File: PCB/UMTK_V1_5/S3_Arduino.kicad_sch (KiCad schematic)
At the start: 30 parts

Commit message: Routing and JLC Assignment Done
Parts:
- removed R2, R3, R6, R7: 10k, Resistor_SMD:R_0402_1005Metric, symbol Device:R_US
- R1, R5: value 10k -> 100k
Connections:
- net VM_Sense: now also R5.2
- net Vin_Sense: now also R1.2
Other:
- moved on the sheet: R1, R5

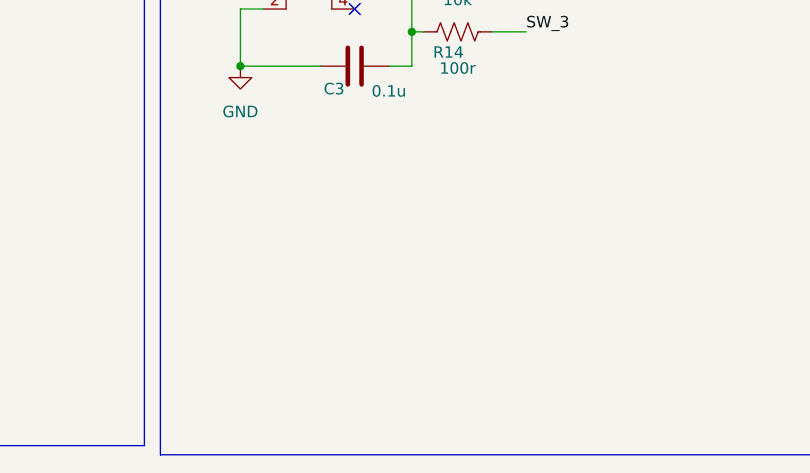
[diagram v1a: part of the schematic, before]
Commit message: Bug fixes and add dummy headers for DFM
Fix:
- Power jack footprint incorrect for high current jack
- Motor and Estop terminal hole size too small
- Added designator and position for arduino headers for DFM
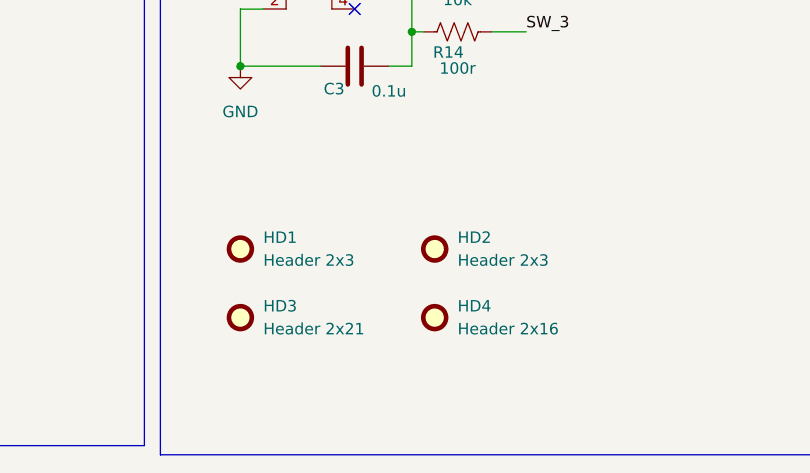
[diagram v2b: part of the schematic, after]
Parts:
- added HD1, HD2: Header 2x3, AMX_Logo:Dummy_Header_2x3, symbol Mechanical:Fiducial
- added HD3: Header 2x21, AMX_Logo:Dummy_Header_2x21, symbol Mechanical:Fiducial
- added HD4: Header 2x16, AMX_Logo:Dummy_Header_2x16, symbol Mechanical:Fiducial

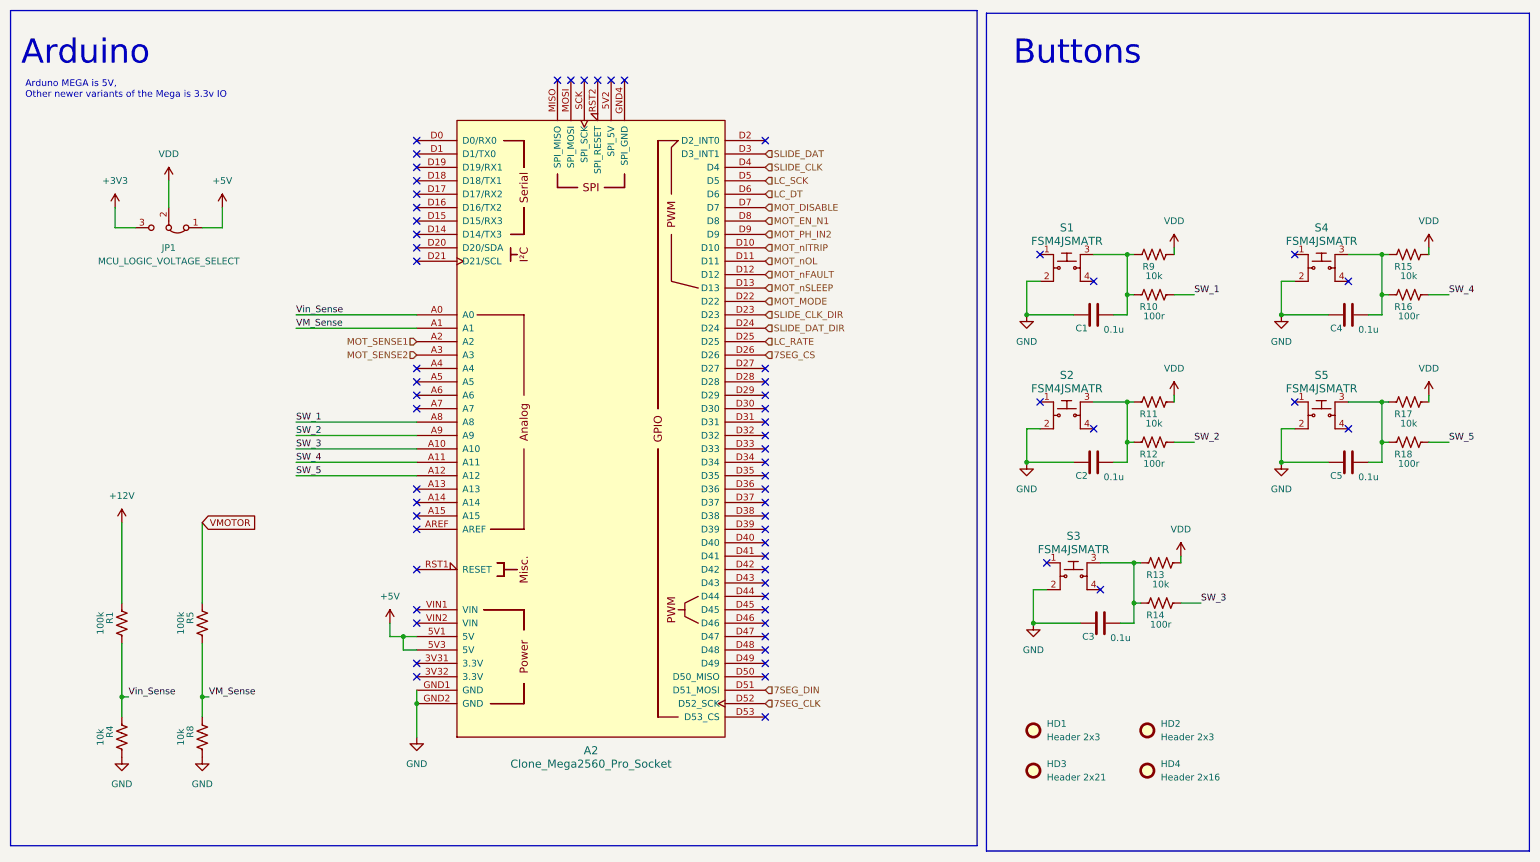
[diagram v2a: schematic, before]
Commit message: Added pin assignment doc for firmware
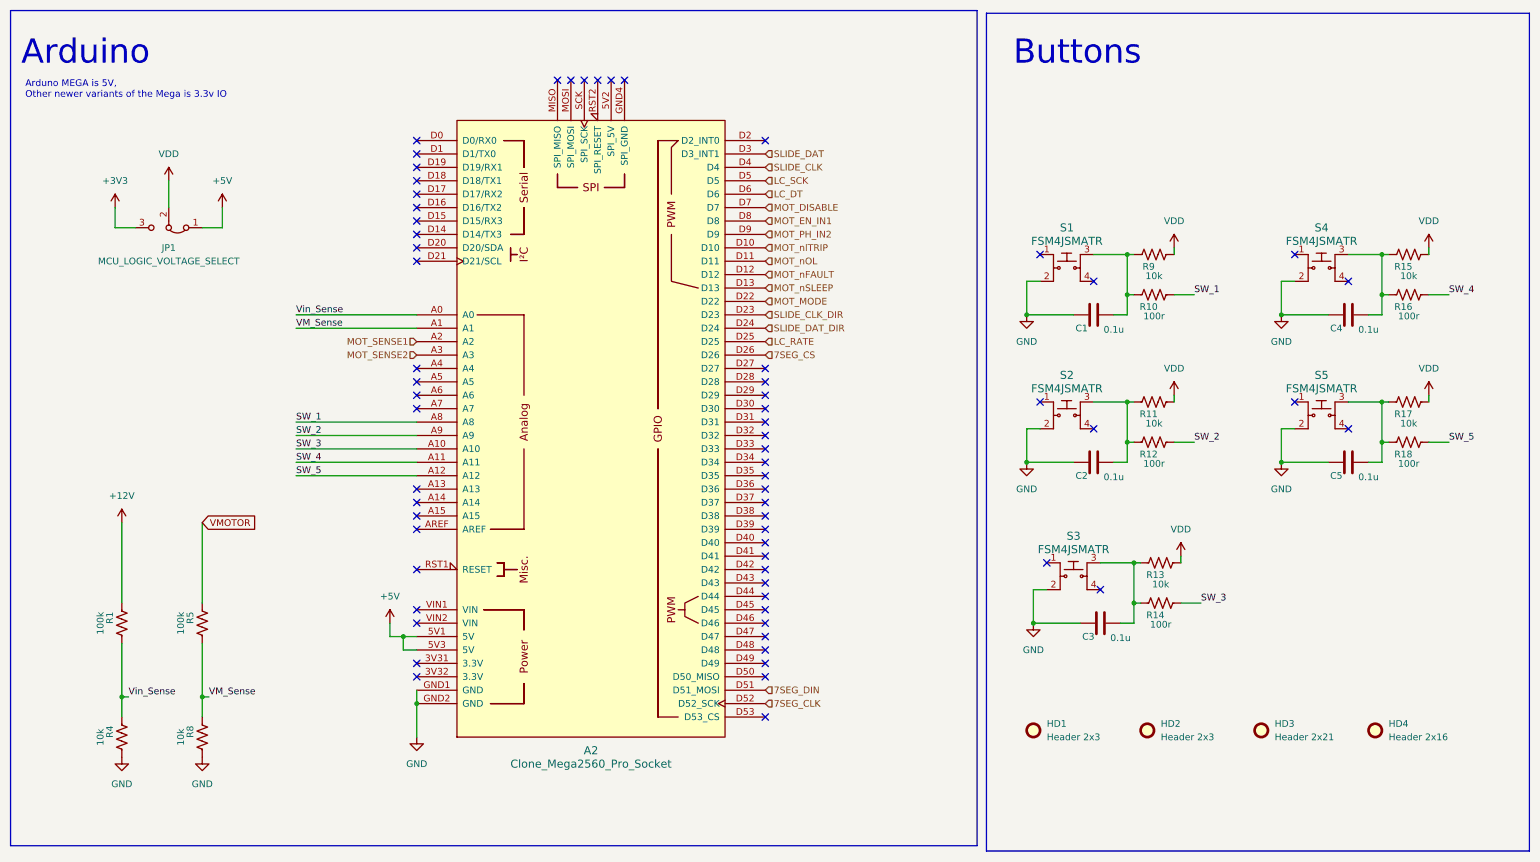
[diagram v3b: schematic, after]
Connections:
- net MOT_EN_N1 renamed MOT_EN_IN1
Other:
- moved on the sheet: HD3, HD4
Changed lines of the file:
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@@
 		)
 	)
-	(hierarchical_label "MOT_EN_N1"
+	(hierarchical_label "MOT_EN_IN1"
 		(shape input)
 		(at 147.32 59.69 0)
@@
 	(symbol
 		(lib_id "Mechanical:Fiducial")
-		(at 219.71 163.83 0)
+		(at 262.89 156.21 0)
 		(unit 1)
 		(exclude_from_sim yes)
@@
 		(fields_autoplaced yes)
 		(property "Reference" "HD4"
-			(at 222.25 162.5599 0)
+			(at 265.43 154.9399 0)
 			(effects
 				(font
@@
 		)
 		(property "Value" "Header 2x16"
-			(at 222.25 165.0999 0)
+			(at 265.43 157.4799 0)
 			(effects
 				(font
@@
 		)
 		(property "Footprint" "AMX_Logo:Dummy_Header_2x16"
-			(at 219.71 163.83 0)
+			(at 262.89 156.21 0)
 			(effects
 				(font
@@
 		)
 		(property "Datasheet" "~"
-			(at 219.71 163.83 0)
+			(at 262.89 156.21 0)
 			(effects
 				(font
@@
 		)
 		(property "Description" "Fiducial Marker"
-			(at 219.71 163.83 0)
+			(at 262.89 156.21 0)
 			(effects
 				(font
@@
 	(symbol
 		(lib_id "Mechanical:Fiducial")
-		(at 198.12 163.83 0)
+		(at 241.3 156.21 0)
 		(unit 1)
 		(exclude_from_sim yes)
@@
 		(fields_autoplaced yes)
 		(property "Reference" "HD3"
-			(at 200.66 162.5599 0)
+			(at 243.84 154.9399 0)
 			(effects
 				(font
@@
 		)
 		(property "Value" "Header 2x21"
-			(at 200.66 165.0999 0)
+			(at 243.84 157.4799 0)
 			(effects
 				(font
@@
 		)
 		(property "Footprint" "AMX_Logo:Dummy_Header_2x21"
-			(at 198.12 163.83 0)
+			(at 241.3 156.21 0)
 			(effects
 				(font
@@
 		)
 		(property "Datasheet" "~"
-			(at 198.12 163.83 0)
+			(at 241.3 156.21 0)
 			(effects
 				(font
@@
 		)
 		(property "Description" "Fiducial Marker"
-			(at 198.12 163.83 0)
-			(effects
-				(font
+			(at 241.3 156.21 0)
+			(effects
+				(font

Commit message: Make simple components bigger
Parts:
- C1, C2, C3, C4, C5: footprint Capacitor_SMD:C_0402_1005Metric -> Capacitor_SMD:C_0603_1608Metric
- R1, R10, R11, R12, R13, R14, R15, R16, R17, R18, R4, R5, R8, R9: footprint Resistor_SMD:R_0402_1005Metric -> Resistor_SMD:R_0603_1608Metric
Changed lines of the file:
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@@
 			)
 		)
-		(property "Footprint" "Resistor_SMD:R_0402_1005Metric"
+		(property "Footprint" "Resistor_SMD:R_0603_1608Metric"
 			(at 222.504 131.064 90)
 			(effects
@@
 			)
 		)
-		(property "Footprint" "Capacitor_SMD:C_0402_1005Metric"
+		(property "Footprint" "Capacitor_SMD:C_0603_1608Metric"
 			(at 261.62 76.5048 0)
 			(effects
@@
 			)
 		)
-		(property "Footprint" "Resistor_SMD:R_0402_1005Metric"
+		(property "Footprint" "Resistor_SMD:R_0603_1608Metric"
 			(at 269.494 65.024 90)
 			(effects
@@
 			)
 		)
-		(property "Footprint" "Resistor_SMD:R_0402_1005Metric"
+		(property "Footprint" "Resistor_SMD:R_0603_1608Metric"
 			(at 26.416 157.734 90)
 			(effects
@@
 			)
 		)
-		(property "Footprint" "Resistor_SMD:R_0402_1005Metric"
+		(property "Footprint" "Resistor_SMD:R_0603_1608Metric"
 			(at 269.494 92.964 90)
 			(effects
@@
 			)
 		)
-		(property "Footprint" "Capacitor_SMD:C_0402_1005Metric"
+		(property "Footprint" "Capacitor_SMD:C_0603_1608Metric"
 			(at 261.62 104.4448 0)
 			(effects
@@
 			)
 		)
-		(property "Footprint" "Capacitor_SMD:C_0402_1005Metric"
+		(property "Footprint" "Capacitor_SMD:C_0603_1608Metric"
 			(at 213.36 76.5048 0)
 			(effects
@@
 			)
 		)
-		(property "Footprint" "Resistor_SMD:R_0402_1005Metric"
+		(property "Footprint" "Resistor_SMD:R_0603_1608Metric"
 			(at 221.234 92.964 90)
 			(effects
@@
 			)
 		)
-		(property "Footprint" "Resistor_SMD:R_0402_1005Metric"
+		(property "Footprint" "Resistor_SMD:R_0603_1608Metric"
 			(at 41.656 157.734 90)
 			(effects
@@
 			)
 		)
-		(property "Footprint" "Resistor_SMD:R_0402_1005Metric"
+		(property "Footprint" "Resistor_SMD:R_0603_1608Metric"
 			(at 269.494 100.584 90)
 			(effects
@@
 			)
 		)
-		(property "Footprint" "Resistor_SMD:R_0402_1005Metric"
+		(property "Footprint" "Resistor_SMD:R_0603_1608Metric"
 			(at 41.656 136.144 90)
 			(effects
@@
 			)
 		)
-		(property "Footprint" "Resistor_SMD:R_0402_1005Metric"
+		(property "Footprint" "Resistor_SMD:R_0603_1608Metric"
 			(at 221.234 100.584 90)
 			(effects
@@
 			)
 		)
-		(property "Footprint" "Capacitor_SMD:C_0402_1005Metric"
+		(property "Footprint" "Capacitor_SMD:C_0603_1608Metric"
 			(at 213.36 104.4448 0)
 			(effects
@@
 			)
 		)
-		(property "Footprint" "Resistor_SMD:R_0402_1005Metric"
+		(property "Footprint" "Resistor_SMD:R_0603_1608Metric"
 			(at 269.494 72.644 90)
 			(effects
@@
 			)
 		)
-		(property "Footprint" "Capacitor_SMD:C_0402_1005Metric"
+		(property "Footprint" "Capacitor_SMD:C_0603_1608Metric"
 			(at 214.63 134.9248 0)
 			(effects
@@
 			)
 		)
-		(property "Footprint" "Resistor_SMD:R_0402_1005Metric"
+		(property "Footprint" "Resistor_SMD:R_0603_1608Metric"
 			(at 222.504 123.444 90)
 			(effects
@@
 			)
 		)
-		(property "Footprint" "Resistor_SMD:R_0402_1005Metric"
+		(property "Footprint" "Resistor_SMD:R_0603_1608Metric"
 			(at 221.234 65.024 90)
 			(effects
@@
 			)
 		)
-		(property "Footprint" "Resistor_SMD:R_0402_1005Metric"
+		(property "Footprint" "Resistor_SMD:R_0603_1608Metric"
 			(at 221.234 72.644 90)
 			(effects
@@
 			)
 		)
-		(property "Footprint" "Resistor_SMD:R_0402_1005Metric"
+		(property "Footprint" "Resistor_SMD:R_0603_1608Metric"
 			(at 26.416 136.144 90)
 			(effects

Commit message: Move interrupr pin to 3, Move motor sleep to 14 so 13 can LED
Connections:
- net MOT_nSLEEP: now also A2.D14 (D14/TX3); no longer A2.D13
- net SLIDE_CLK: now also A2.D3 (D3_INT1); no longer A2.D4
- net SLIDE_DAT: now also A2.D4; no longer A2.D3 (D3_INT1)
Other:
- note added: "SLIDE REQUIRE INTERRUPT ON MEGA ONLY THESE PINS CAN INTERRUPT: 2, 3, 18, 19"
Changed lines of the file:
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@@
+	)
+	(no_connect
+		(at 147.32 87.63)
 	)
 	(no_connect
@@
 	)
 	(no_connect
-		(at 147.32 87.63)
-	)
-	(no_connect
 		(at 247.65 66.04)
 	)
@@
 	)
 	(no_connect
+		(at 147.32 72.39)
+	)
+	(no_connect
 		(at 147.32 128.27)
 	)
@@
 	(no_connect
 		(at 113.03 33.02)
-	)
-	(no_connect
-		(at 81.28 62.23)
 	)
 	(wire
@@
 		)
 	)
+	(text "SLIDE REQUIRE INTERRUPT\nON MEGA ONLY THESE PINS\nCAN INTERRUPT:\n2, 3, 18, 19"
+		(exclude_from_sim no)
+		(at 149.606 32.258 0)
+		(effects
+			(font
+				(size 1.27 1.27)
+			)
+			(justify left)
+		)
+	)
 	(text "Buttons"
 		(exclude_from_sim no)
@@
 	(label "SW_2"
 		(at 228.6 101.6 0)
+		(fields_autoplaced yes)
+		(effects
+			(font
+				(size 1.27 1.27)
+			)
+			(justify left bottom)
+		)
+	)
+	(label "13 IS INDICATOR LED"
+		(at 148.59 73.66 0)
 		(fields_autoplaced yes)
 		(effects
@@
 		)
 	)
+	(hierarchical_label "SLIDE_CLK"
+		(shape input)
+		(at 147.32 46.99 0)
+		(fields_autoplaced yes)
+		(effects
+			(font
+				(size 1.27 1.27)
+			)
+			(justify left)
+		)
+	)
 	(hierarchical_label "MOT_MODE"
 		(shape input)
@@
 		)
 	)
-	(hierarchical_label "SLIDE_CLK"
+	(hierarchical_label "MOT_SENSE2"
+		(shape input)
+		(at 81.28 85.09 180)
+		(fields_autoplaced yes)
+		(effects
+			(font
+				(size 1.27 1.27)
+			)
+			(justify right)
+		)
+	)
+	(hierarchical_label "7SEG_CLK"
+		(shape input)
+		(at 147.32 151.13 0)
+		(fields_autoplaced yes)
+		(effects
+			(font
+				(size 1.27 1.27)
+			)
+			(justify left)
+		)
+	)
+	(hierarchical_label "LC_DT"
+		(shape input)
+		(at 147.32 54.61 0)
+		(fields_autoplaced yes)
+		(effects
+			(font
+				(size 1.27 1.27)
+			)
+			(justify left)
+		)
+	)
+	(hierarchical_label "SLIDE_DAT"
 		(shape input)
 		(at 147.32 49.53 0)
@@
 		)
 	)
-	(hierarchical_label "MOT_SENSE2"
-		(shape input)
-		(at 81.28 85.09 180)
+	(hierarchical_label "SLIDE_CLK_DIR"
+		(shape input)
+		(at 147.32 77.47 0)
+		(fields_autoplaced yes)
+		(effects
+			(font
+				(size 1.27 1.27)
+			)
+			(justify left)
+		)
+	)
+	(hierarchical_label "SLIDE_DAT_DIR"
+		(shape input)
+		(at 147.32 80.01 0)
+		(fields_autoplaced yes)
+		(effects
+			(font
+				(size 1.27 1.27)
+			)
+			(justify left)
+		)
+	)
+	(hierarchical_label "LC_SCK"
+		(shape input)
+		(at 147.32 52.07 0)
+		(fields_autoplaced yes)
+		(effects
+			(font
+				(size 1.27 1.27)
+			)
+			(justify left)
+		)
+	)
+	(hierarchical_label "MOT_nOL"
+		(shape input)
+		(at 147.32 67.31 0)
+		(fields_autoplaced yes)
+		(effects
+			(font
+				(size 1.27 1.27)
+			)
+			(justify left)
+		)
+	)
+	(hierarchical_label "7SEG_CS"
+		(shape input)
+		(at 147.32 85.09 0)
+		(fields_autoplaced yes)
+		(effects
+			(font
+				(size 1.27 1.27)
+			)
+			(justify left)
+		)
+	)
+	(hierarchical_label "LC_RATE"
+		(shape input)
+		(at 147.32 82.55 0)
+		(fields_autoplaced yes)
+		(effects
+			(font
+				(size 1.27 1.27)
+			)
+			(justify left)
+		)
+	)
+	(hierarchical_label "MOT_DISABLE"
+		(shape input)
+		(at 147.32 57.15 0)
+		(fields_autoplaced yes)
+		(effects
+			(font
+				(size 1.27 1.27)
+			)
+			(justify left)
+		)
+	)
+	(hierarchical_label "7SEG_DIN"
+		(shape input)
+		(at 147.32 148.59 0)
+		(fields_autoplaced yes)
+		(effects
+			(font
+				(size 1.27 1.27)
+			)
+			(justify left)
+		)
+	)
+	(hierarchical_label "MOT_EN_IN1"
+		(shape input)
+		(at 147.32 59.69 0)
+		(fields_autoplaced yes)
+		(effects
+			(font
+				(size 1.27 1.27)
+			)
+			(justify left)
+		)
+	)
+	(hierarchical_label "MOT_nSLEEP"
+		(shape input)
+		(at 81.28 62.23 180)
 		(fields_autoplaced yes)
 		(effects
@@
 		)
 	)
-	(hierarchical_label "7SEG_CLK"
-		(shape input)
-		(at 147.32 151.13 0)
-		(fields_autoplaced yes)
-		(effects
-			(font
-				(size 1.27 1.27)
-			)
-			(justify left)
-		)
-	)
-	(hierarchical_label "LC_DT"
-		(shape input)
-		(at 147.32 54.61 0)
-		(fields_autoplaced yes)
-		(effects
-			(font
-				(size 1.27 1.27)
-			)
-			(justify left)
-		)
-	)
-	(hierarchical_label "MOT_nSLEEP"
-		(shape input)
-		(at 147.32 72.39 0)
-		(fields_autoplaced yes)
-		(effects
-			(font
-				(size 1.27 1.27)
-			)
-			(justify left)
-		)
-	)
-	(hierarchical_label "SLIDE_CLK_DIR"
-		(shape input)
-		(at 147.32 77.47 0)
-		(fields_autoplaced yes)
-		(effects
-			(font
-				(size 1.27 1.27)
-			)
-			(justify left)
-		)
-	)
-	(hierarchical_label "SLIDE_DAT_DIR"
-		(shape input)
-		(at 147.32 80.01 0)
-		(fields_autoplaced yes)
-		(effects
-			(font
-				(size 1.27 1.27)
-			)
-			(justify left)
-		)
-	)
-	(hierarchical_label "LC_SCK"
-		(shape input)
-		(at 147.32 52.07 0)
-		(fields_autoplaced yes)
-		(effects
-			(font
-				(size 1.27 1.27)
-			)
-			(justify left)
-		)
-	)
-	(hierarchical_label "MOT_nOL"
-		(shape input)
-		(at 147.32 67.31 0)
-		(fields_autoplaced yes)
-		(effects
-			(font
-				(size 1.27 1.27)
-			)
-			(justify left)
-		)
-	)
-	(hierarchical_label "7SEG_CS"
-		(shape input)
-		(at 147.32 85.09 0)
-		(fields_autoplaced yes)
-		(effects
-			(font
-				(size 1.27 1.27)
-			)
-			(justify left)
-		)
-	)
-	(hierarchical_label "LC_RATE"
-		(shape input)
-		(at 147.32 82.55 0)
-		(fields_autoplaced yes)
-		(effects
-			(font
-				(size 1.27 1.27)
-			)
-			(justify left)
-		)
-	)
-	(hierarchical_label "MOT_DISABLE"
-		(shape input)
-		(at 147.32 57.15 0)
-		(fields_autoplaced yes)
-		(effects
-			(font
-				(size 1.27 1.27)
-			)
-			(justify left)
-		)
-	)
-	(hierarchical_label "7SEG_DIN"
-		(shape input)
-		(at 147.32 148.59 0)
-		(fields_autoplaced yes)
-		(effects
-			(font
-				(size 1.27 1.27)
-			)
-			(justify left)
-		)
-	)
-	(hierarchical_label "MOT_EN_IN1"
-		(shape input)
-		(at 147.32 59.69 0)
-		(fields_autoplaced yes)
-		(effects
-			(font
-				(size 1.27 1.27)
-			)
-			(justify left)
-		)
-	)
 	(hierarchical_label "MOT_PH_IN2"
 		(shape input)
@@
 		(fields_autoplaced yes)
 		(effects
-			(font
-				(size 1.27 1.27)
-			)
-			(justify left)
-		)
-	)
-	(hierarchical_label "SLIDE_DAT"
-		(shape input)
-		(at 147.32 46.99 0)
-		(fields_autoplaced yes)
-		(effects
